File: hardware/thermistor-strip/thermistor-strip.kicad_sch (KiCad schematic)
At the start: 0 parts

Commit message: fix footprint for thermistor strip connector
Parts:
- added J1: FH19C-7S-0.5SH10, Hirose_FH19C_7S_0_5SH:CONN7_FH19C_7S_HIR, symbol Hirose_FH19C_7S_0_5SH:FH19C-7S-0.5SH10
- added RT1, RT2, RT3, RT4, RT5, RT6: NCU18XH103F60RB, Murata_NCU18XH103F60RB:THRMC1608X95N, symbol Murata_NCU18XH103F60RB:NCU18XH103F60RB
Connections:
- new net: J1.3, RT3.1
- new net: J1.1, RT1.1
- new net: J1.2, RT2.1
- new net: J1.4, RT4.1
- new net: J1.5, RT5.1
- new net: J1.6, RT6.1
- new net GND: J1.7, RT1.2, RT2.2, RT3.2, RT4.2, RT5.2, RT6.2

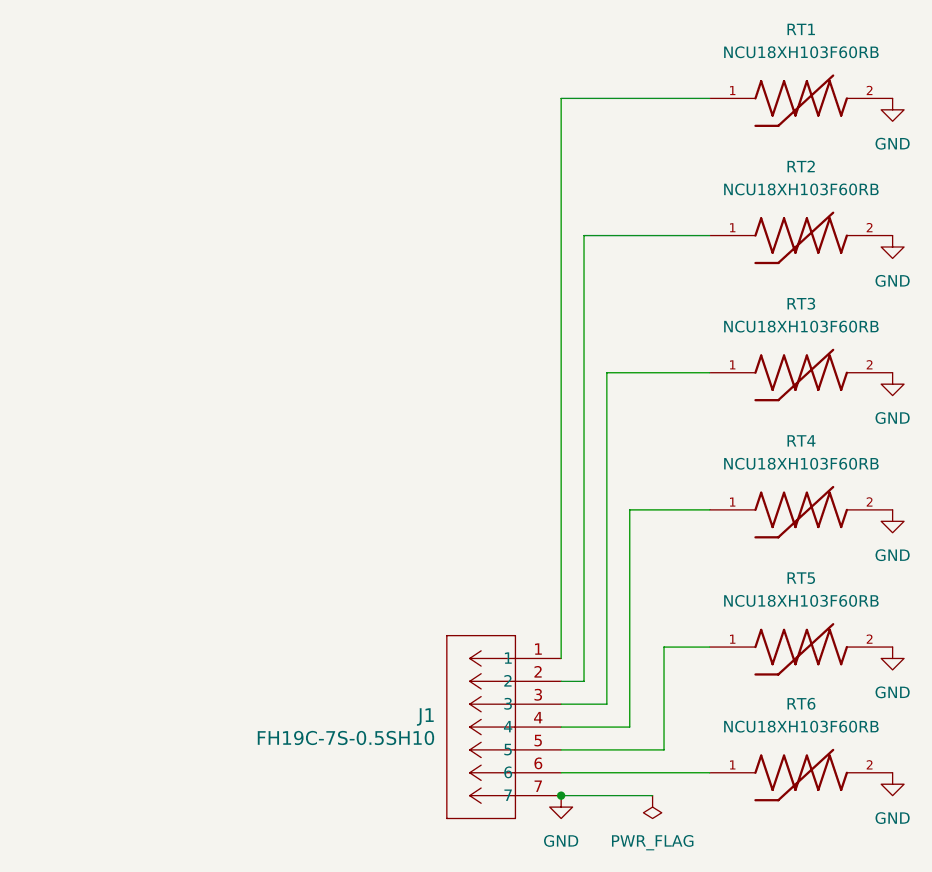
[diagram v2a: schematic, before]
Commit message: Initial thermistor pcb cuts and placement
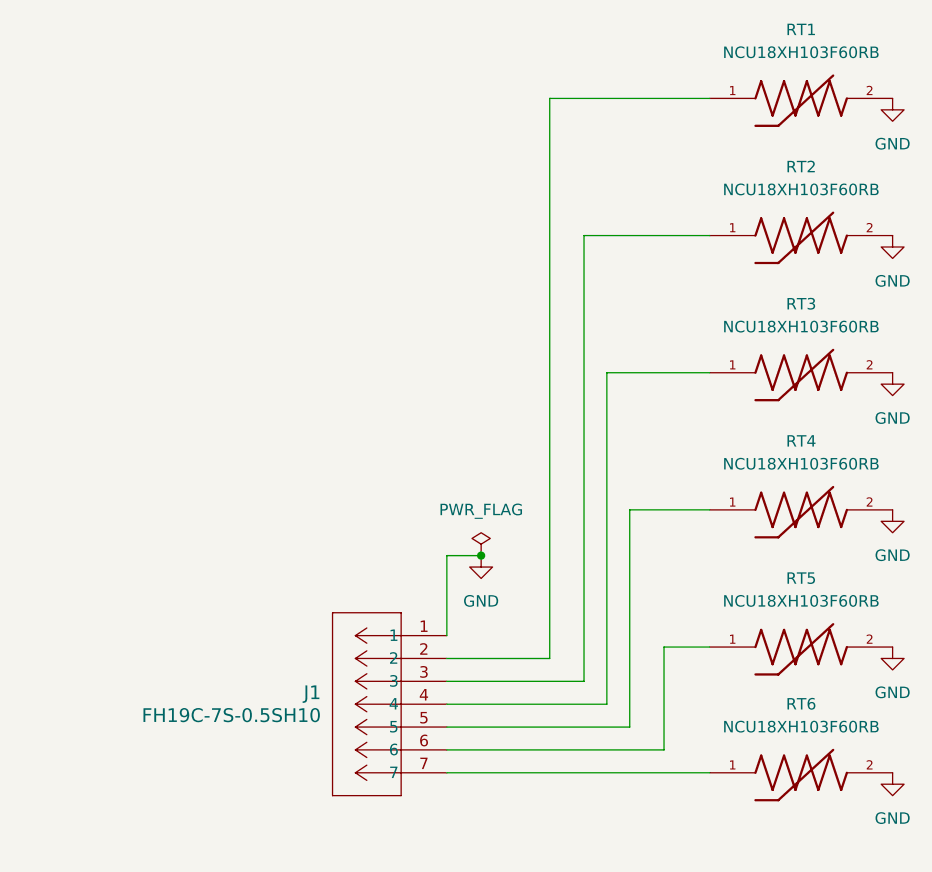
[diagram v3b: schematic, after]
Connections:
- net GND: now also J1.1; no longer J1.7
- net at RT3.1: now also J1.4; no longer J1.3
- net at RT1.1: now also J1.2; no longer J1.1
- net at RT2.1: now also J1.3; no longer J1.2
- net at RT4.1: now also J1.5; no longer J1.4
- net at RT5.1: now also J1.6; no longer J1.5
- net at RT6.1: now also J1.7; no longer J1.6
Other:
- moved on the sheet: J1
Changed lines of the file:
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@@
 	(paper "A4")
 	(junction
-		(at 96.52 121.92)
+		(at 87.63 95.25)
 		(diameter 0)
 		(color 0 0 0 0)
@@
 	(wire
 		(pts
-			(xy 96.52 119.38) (xy 113.03 119.38)
-		)
-		(stroke
-			(width 0)
-			(type default)
-		)
-	)
-	(wire
-		(pts
-			(xy 96.52 109.22) (xy 99.06 109.22)
-		)
-		(stroke
-			(width 0)
-			(type default)
-		)
-	)
-	(wire
-		(pts
-			(xy 96.52 114.3) (xy 104.14 114.3)
+			(xy 83.82 111.76) (xy 101.6 111.76)
+		)
+		(stroke
+			(width 0)
+			(type default)
+		)
+	)
+	(wire
+		(pts
+			(xy 83.82 119.38) (xy 113.03 119.38)
+		)
+		(stroke
+			(width 0)
+			(type default)
+		)
+	)
+	(wire
+		(pts
+			(xy 83.82 114.3) (xy 104.14 114.3)
 		)
 		(stroke
@@
 	(wire
 		(pts
-			(xy 101.6 111.76) (xy 101.6 74.93)
+			(xy 101.6 74.93) (xy 101.6 111.76)
+		)
+		(stroke
+			(width 0)
+			(type default)
+		)
+	)
+	(wire
+		(pts
+			(xy 83.82 95.25) (xy 87.63 95.25)
+		)
+		(stroke
+			(width 0)
+			(type default)
+		)
+	)
+	(wire
+		(pts
+			(xy 83.82 116.84) (xy 107.95 116.84)
 		)
 		(stroke
@@
 	(wire
 		(pts
+			(xy 83.82 109.22) (xy 99.06 109.22)
+		)
+		(stroke
+			(width 0)
+			(type default)
+		)
+	)
+	(wire
+		(pts
 			(xy 104.14 114.3) (xy 104.14 90.17)
 		)
@@
 	(wire
 		(pts
-			(xy 96.52 121.92) (xy 106.68 121.92)
-		)
-		(stroke
-			(width 0)
-			(type default)
-		)
-	)
-	(wire
-		(pts
-			(xy 96.52 111.76) (xy 101.6 111.76)
+			(xy 83.82 106.68) (xy 95.25 106.68)
 		)
 		(stroke
@@
 	(wire
 		(pts
-			(xy 96.52 44.45) (xy 113.03 44.45)
+			(xy 95.25 44.45) (xy 113.03 44.45)
 		)
 		(stroke
@@
 	(wire
 		(pts
-			(xy 96.52 106.68) (xy 96.52 44.45)
-		)
-		(stroke
-			(width 0)
-			(type default)
-		)
-	)
-	(wire
-		(pts
-			(xy 96.52 116.84) (xy 107.95 116.84)
+			(xy 83.82 95.25) (xy 83.82 104.14)
+		)
+		(stroke
+			(width 0)
+			(type default)
+		)
+	)
+	(wire
+		(pts
+			(xy 95.25 106.68) (xy 95.25 44.45)
 		)
 		(stroke
@@
 	(symbol
 		(lib_id "power:PWR_FLAG")
-		(at 106.68 121.92 0)
-		(mirror x)
+		(at 87.63 95.25 0)
+		(mirror y)
 		(unit 1)
 		(body_style 1)
@@
 		(fields_autoplaced yes)
 		(property "Reference" "#FLG01"
-			(at 106.68 123.825 0)
+			(at 87.63 93.345 0)
 			(hide yes)
 			(show_name no)
@@
 		)
 		(property "Value" "PWR_FLAG"
-			(at 106.68 127 0)
+			(at 87.63 90.17 0)
 			(show_name no)
 			(do_not_autoplace no)
@@
 		)
 		(property "Footprint" ""
-			(at 106.68 121.92 0)
+			(at 87.63 95.25 0)
 			(hide yes)
 			(show_name no)
@@
 		)
 		(property "Datasheet" ""
-			(at 106.68 121.92 0)
+			(at 87.63 95.25 0)
 			(hide yes)
 			(show_name no)
@@
 		)
 		(property "Description" "Special symbol for telling ERC where power comes from"
-			(at 106.68 121.92 0)
+			(at 87.63 95.25 0)
 			(hide yes)
 			(show_name no)
@@
 	(symbol
 		(lib_id "Hirose_FH19C_7S_0_5SH:FH19C-7S-0.5SH10")
-		(at 96.52 106.68 0)
+		(at 83.82 104.14 0)
 		(mirror y)
 		(unit 1)
@@
 		(fields_autoplaced yes)
 		(property "Reference" "J1"
-			(at 82.55 113.0299 0)
+			(at 69.85 110.4899 0)
 			(show_name no)
 			(do_not_autoplace no)
@@
 		)
 		(property "Value" "FH19C-7S-0.5SH10"
-			(at 82.55 115.5699 0)
+			(at 69.85 113.0299 0)
 			(show_name no)
 			(do_not_autoplace no)
@@
 		)
 		(property "Footprint" "Hirose_FH19C_7S_0_5SH:CONN7_FH19C_7S_HIR"
-			(at 96.52 106.68 0)
+			(at 83.82 104.14 0)
 			(hide yes)
 			(show_name no)
@@
 		)
 		(property "Datasheet" "FH19C-7S-0.5SH10"
-			(at 96.52 106.68 0)
+			(at 83.82 104.14 0)
 			(hide yes)
 			(show_name no)
@@
 		)
 		(property "Description" ""
-			(at 96.52 106.68 0)
+			(at 83.82 104.14 0)
 			(hide yes)
 			(show_name no)
@@
 	(symbol
 		(lib_id "power:GND")
-		(at 96.52 121.92 0)
+		(at 87.63 95.25 0)
 		(unit 1)
 		(body_style 1)
@@
 		(fields_autoplaced yes)
 		(property "Reference" "#PWR01"
-			(at 96.52 128.27 0)
+			(at 87.63 101.6 0)
 			(hide yes)
 			(show_name no)
@@
 		)
 		(property "Value" "GND"
-			(at 96.52 127 0)
+			(at 87.63 100.33 0)
 			(show_name no)
 			(do_not_autoplace no)
@@
 		)
 		(property "Footprint" ""
-			(at 96.52 121.92 0)
+			(at 87.63 95.25 0)
 			(hide yes)
 			(show_name no)
@@
 		)
 		(property "Datasheet" ""
-			(at 96.52 121.92 0)
+			(at 87.63 95.25 0)
 			(hide yes)
 			(show_name no)
@@
 		)
 		(property "Description" "Power symbol creates a global label with name \"GND\" , ground"
-			(at 96.52 121.92 0)
-			(hide yes)
-			(show_name no)
+			(at 87.63 95.25 0)
+			(hide yes)
+			(show_name no)

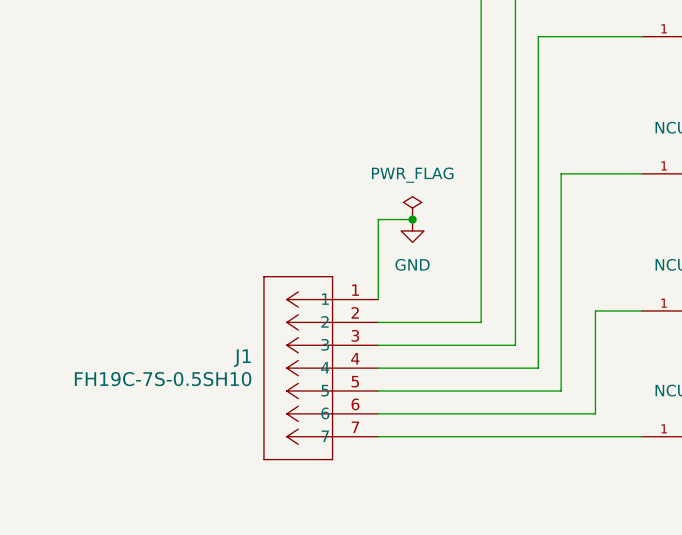
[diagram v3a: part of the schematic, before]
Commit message: update placement of connector and invert pins for thermistors for more organized traces
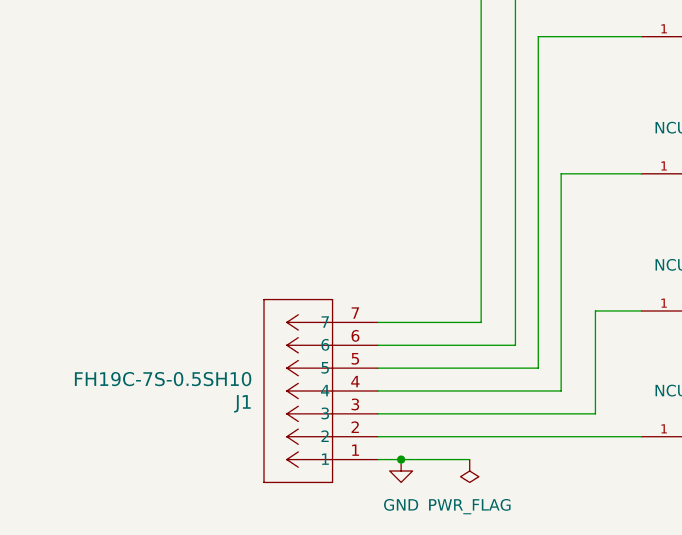
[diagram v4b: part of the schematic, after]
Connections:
- net at RT3.1: now also J1.5; no longer J1.4
- net at J1.2: now also RT6.1; no longer RT1.1
- net at J1.3: now also RT5.1; no longer RT2.1
- net at RT4.1: now also J1.4; no longer J1.5
- net at J1.6: now also RT2.1; no longer RT5.1
- net at J1.7: now also RT1.1; no longer RT6.1
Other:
- moved on the sheet: J1
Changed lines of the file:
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@@
 	(paper "A4")
 	(junction
-		(at 87.63 95.25)
+		(at 86.36 121.92)
 		(diameter 0)
 		(color 0 0 0 0)
@@
 	(wire
 		(pts
-			(xy 83.82 95.25) (xy 87.63 95.25)
+			(xy 83.82 121.92) (xy 93.98 121.92)
 		)
 		(stroke
@@
 		(pts
 			(xy 99.06 59.69) (xy 113.03 59.69)
-		)
-		(stroke
-			(width 0)
-			(type default)
-		)
-	)
-	(wire
-		(pts
-			(xy 83.82 95.25) (xy 83.82 104.14)
 		)
 		(stroke
@@
 	(symbol
 		(lib_id "power:PWR_FLAG")
-		(at 87.63 95.25 0)
-		(mirror y)
+		(at 93.98 121.92 0)
+		(mirror x)
 		(unit 1)
 		(body_style 1)
@@
 		(fields_autoplaced yes)
 		(property "Reference" "#FLG01"
-			(at 87.63 93.345 0)
+			(at 93.98 123.825 0)
 			(hide yes)
 			(show_name no)
@@
 		)
 		(property "Value" "PWR_FLAG"
-			(at 87.63 90.17 0)
+			(at 93.98 127 0)
 			(show_name no)
 			(do_not_autoplace no)
@@
 		)
 		(property "Footprint" ""
-			(at 87.63 95.25 0)
+			(at 93.98 121.92 0)
 			(hide yes)
 			(show_name no)
@@
 		)
 		(property "Datasheet" ""
-			(at 87.63 95.25 0)
+			(at 93.98 121.92 0)
 			(hide yes)
 			(show_name no)
@@
 		)
 		(property "Description" "Special symbol for telling ERC where power comes from"
-			(at 87.63 95.25 0)
+			(at 93.98 121.92 0)
 			(hide yes)
 			(show_name no)
@@
 	(symbol
 		(lib_id "Hirose_FH19C_7S_0_5SH:FH19C-7S-0.5SH10")
-		(at 83.82 104.14 0)
-		(mirror y)
+		(at 83.82 121.92 180)
 		(unit 1)
 		(body_style 1)
@@
 		(fields_autoplaced yes)
 		(property "Reference" "J1"
-			(at 69.85 110.4899 0)
+			(at 69.85 115.5701 0)
 			(show_name no)
 			(do_not_autoplace no)
@@
 		)
 		(property "Value" "FH19C-7S-0.5SH10"
-			(at 69.85 113.0299 0)
+			(at 69.85 113.0301 0)
 			(show_name no)
 			(do_not_autoplace no)
@@
 		)
 		(property "Footprint" "Hirose_FH19C_7S_0_5SH:CONN7_FH19C_7S_HIR"
-			(at 83.82 104.14 0)
+			(at 83.82 121.92 0)
 			(hide yes)
 			(show_name no)
@@
 		)
 		(property "Datasheet" "FH19C-7S-0.5SH10"
-			(at 83.82 104.14 0)
+			(at 83.82 121.92 0)
 			(hide yes)
 			(show_name no)
@@
 		)
 		(property "Description" ""
-			(at 83.82 104.14 0)
+			(at 83.82 121.92 0)
 			(hide yes)
 			(show_name no)
@@
 	(symbol
 		(lib_id "power:GND")
-		(at 87.63 95.25 0)
+		(at 86.36 121.92 0)
 		(unit 1)
 		(body_style 1)
@@
 		(fields_autoplaced yes)
 		(property "Reference" "#PWR01"
-			(at 87.63 101.6 0)
+			(at 86.36 128.27 0)
 			(hide yes)
 			(show_name no)
@@
 		)
 		(property "Value" "GND"
-			(at 87.63 100.33 0)
+			(at 86.36 127 0)
 			(show_name no)
 			(do_not_autoplace no)
@@
 		)
 		(property "Footprint" ""
-			(at 87.63 95.25 0)
+			(at 86.36 121.92 0)
 			(hide yes)
 			(show_name no)
@@
 		)
 		(property "Datasheet" ""
-			(at 87.63 95.25 0)
+			(at 86.36 121.92 0)
 			(hide yes)
 			(show_name no)
@@
 		)
 		(property "Description" "Power symbol creates a global label with name \"GND\" , ground"
-			(at 87.63 95.25 0)
-			(hide yes)
-			(show_name no)
+			(at 86.36 121.92 0)
+			(hide yes)
+			(show_name no)

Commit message: initial tracing progress
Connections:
- net GND: now also J1.7; no longer J1.1
- net at RT3.1: now also J1.3; no longer J1.5
- net at J1.2: now also RT2.1; no longer RT6.1
- net at RT5.1: now also J1.5; no longer J1.3
- net at J1.6: now also RT6.1; no longer RT2.1
- net at RT1.1: now also J1.1; no longer J1.7
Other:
- moved on the sheet: J1
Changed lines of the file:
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@@
 	(paper "A4")
 	(junction
-		(at 86.36 121.92)
+		(at 82.55 121.92)
 		(diameter 0)
 		(color 0 0 0 0)
@@
 	(wire
 		(pts
-			(xy 83.82 111.76) (xy 101.6 111.76)
-		)
-		(stroke
-			(width 0)
-			(type default)
-		)
-	)
-	(wire
-		(pts
-			(xy 83.82 119.38) (xy 113.03 119.38)
-		)
-		(stroke
-			(width 0)
-			(type default)
-		)
-	)
-	(wire
-		(pts
-			(xy 83.82 114.3) (xy 104.14 114.3)
+			(xy 76.2 121.92) (xy 82.55 121.92)
+		)
+		(stroke
+			(width 0)
+			(type default)
+		)
+	)
+	(wire
+		(pts
+			(xy 76.2 114.3) (xy 104.14 114.3)
+		)
+		(stroke
+			(width 0)
+			(type default)
+		)
+	)
+	(wire
+		(pts
+			(xy 76.2 116.84) (xy 107.95 116.84)
 		)
 		(stroke
@@
 	(wire
 		(pts
-			(xy 83.82 121.92) (xy 93.98 121.92)
-		)
-		(stroke
-			(width 0)
-			(type default)
-		)
-	)
-	(wire
-		(pts
-			(xy 83.82 116.84) (xy 107.95 116.84)
-		)
-		(stroke
-			(width 0)
-			(type default)
-		)
-	)
-	(wire
-		(pts
 			(xy 107.95 105.41) (xy 113.03 105.41)
 		)
@@
 	(wire
 		(pts
-			(xy 83.82 109.22) (xy 99.06 109.22)
-		)
-		(stroke
-			(width 0)
-			(type default)
-		)
-	)
-	(wire
-		(pts
 			(xy 104.14 114.3) (xy 104.14 90.17)
 		)
@@
 	(wire
 		(pts
+			(xy 82.55 121.92) (xy 90.17 121.92)
+		)
+		(stroke
+			(width 0)
+			(type default)
+		)
+	)
+	(wire
+		(pts
+			(xy 76.2 119.38) (xy 113.03 119.38)
+		)
+		(stroke
+			(width 0)
+			(type default)
+		)
+	)
+	(wire
+		(pts
 			(xy 101.6 74.93) (xy 113.03 74.93)
 		)
@@
 	(wire
 		(pts
-			(xy 83.82 106.68) (xy 95.25 106.68)
-		)
-		(stroke
-			(width 0)
-			(type default)
-		)
-	)
-	(wire
-		(pts
 			(xy 104.14 90.17) (xy 113.03 90.17)
 		)
@@
 	(wire
 		(pts
+			(xy 76.2 111.76) (xy 101.6 111.76)
+		)
+		(stroke
+			(width 0)
+			(type default)
+		)
+	)
+	(wire
+		(pts
 			(xy 95.25 106.68) (xy 95.25 44.45)
+		)
+		(stroke
+			(width 0)
+			(type default)
+		)
+	)
+	(wire
+		(pts
+			(xy 76.2 109.22) (xy 99.06 109.22)
+		)
+		(stroke
+			(width 0)
+			(type default)
+		)
+	)
+	(wire
+		(pts
+			(xy 76.2 106.68) (xy 95.25 106.68)
 		)
 		(stroke
@@
 	(symbol
 		(lib_id "power:PWR_FLAG")
-		(at 93.98 121.92 0)
+		(at 90.17 121.92 0)
 		(mirror x)
 		(unit 1)
@@
 		(fields_autoplaced yes)
 		(property "Reference" "#FLG01"
-			(at 93.98 123.825 0)
+			(at 90.17 123.825 0)
 			(hide yes)
 			(show_name no)
@@
 		)
 		(property "Value" "PWR_FLAG"
-			(at 93.98 127 0)
+			(at 90.17 127 0)
 			(show_name no)
 			(do_not_autoplace no)
@@
 		)
 		(property "Footprint" ""
-			(at 93.98 121.92 0)
+			(at 90.17 121.92 0)
 			(hide yes)
 			(show_name no)
@@
 		)
 		(property "Datasheet" ""
-			(at 93.98 121.92 0)
+			(at 90.17 121.92 0)
 			(hide yes)
 			(show_name no)
@@
 		)
 		(property "Description" "Special symbol for telling ERC where power comes from"
-			(at 93.98 121.92 0)
+			(at 90.17 121.92 0)
 			(hide yes)
 			(show_name no)
@@
 	(symbol
 		(lib_id "Hirose_FH19C_7S_0_5SH:FH19C-7S-0.5SH10")
-		(at 83.82 121.92 180)
+		(at 76.2 106.68 0)
+		(mirror y)
 		(unit 1)
 		(body_style 1)
@@
 		(fields_autoplaced yes)
 		(property "Reference" "J1"
-			(at 69.85 115.5701 0)
+			(at 62.23 113.0299 0)
 			(show_name no)
 			(do_not_autoplace no)
@@
 		)
 		(property "Value" "FH19C-7S-0.5SH10"
-			(at 69.85 113.0301 0)
+			(at 62.23 115.5699 0)
 			(show_name no)
 			(do_not_autoplace no)
@@
 		)
 		(property "Footprint" "Hirose_FH19C_7S_0_5SH:CONN7_FH19C_7S_HIR"
-			(at 83.82 121.92 0)
+			(at 76.2 106.68 0)
 			(hide yes)
 			(show_name no)
@@
 		)
 		(property "Datasheet" "FH19C-7S-0.5SH10"
-			(at 83.82 121.92 0)
+			(at 76.2 106.68 0)
 			(hide yes)
 			(show_name no)
@@
 		)
 		(property "Description" ""
-			(at 83.82 121.92 0)
+			(at 76.2 106.68 0)
 			(hide yes)
 			(show_name no)
@@
 	(symbol
 		(lib_id "power:GND")
-		(at 86.36 121.92 0)
+		(at 82.55 121.92 0)
 		(unit 1)
 		(body_style 1)
@@
 		(fields_autoplaced yes)
 		(property "Reference" "#PWR01"
-			(at 86.36 128.27 0)
+			(at 82.55 128.27 0)
 			(hide yes)
 			(show_name no)
@@
 		)
 		(property "Value" "GND"
-			(at 86.36 127 0)
+			(at 82.55 127 0)
 			(show_name no)
 			(do_not_autoplace no)
@@
 		)
 		(property "Footprint" ""
-			(at 86.36 121.92 0)
+			(at 82.55 121.92 0)
 			(hide yes)
 			(show_name no)
@@
 		)
 		(property "Datasheet" ""
-			(at 86.36 121.92 0)
+			(at 82.55 121.92 0)
 			(hide yes)
 			(show_name no)
@@
 		)
 		(property "Description" "Power symbol creates a global label with name \"GND\" , ground"
-			(at 86.36 121.92 0)
-			(hide yes)
-			(show_name no)
+			(at 82.55 121.92 0)
+			(hide yes)
+			(show_name no)
